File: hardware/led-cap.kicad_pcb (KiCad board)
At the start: 2 copper layers, 76.2 x 50.8 mm, 10 parts, among them IC1 ATTINY20-X, K1 CONN_3, P1 CONN_2, P2 CONN_6, Q1 IRLML2402PbF, U1 MMA7660

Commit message: Cleanup and PCB Layout
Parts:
- C1, C2: footprint SMD_Packages:SM0805 -> SM0805
- IC1: footprint SMD_Packages:TSSOP16 -> TSSOP16
- K1: footprint Connect:SIL-3 -> SIL-3
- P1: footprint Connect:SIL-2 -> SIL-2
- P2: footprint Connect:SIL-6 -> SIL-6
- Q1: footprint SMD_Packages:SOT23 -> SOT23
- R1, R2: footprint SMD_Packages:SM0603 -> SM0603
- U1: footprint tom:DFN-10 -> DFN10
- moved R2 98.3 mm to (61.0, 71.1)
- moved P2 90.3 mm to (55.2, 78.7), turned to 90 degrees
- moved U1 88.1 mm to (66.8, 69.5), turned to 180 degrees
- moved P1 86.8 mm to (75.7, 63.4)
- moved C2 85.4 mm to (75.7, 69.5)
- moved C1 84.6 mm to (75.7, 67.2)
- moved IC1 80.2 mm to (66.8, 77.0)
- moved R1 80.0 mm to (61.0, 73.9)
- moved Q1 76.2 mm to (77.0, 74.9), turned to 270 degrees
- moved K1 67.2 mm to (82.4, 71.1), turned to 270 degrees
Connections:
- IC1 pad 2: Net-(IC1-Pad2) -> (no net)
- IC1 pad 7: Net-(IC1-Pad7) -> (no net)
- IC1 pad 8: Net-(IC1-Pad8) -> (no net)
- U1 pad 1: Net-(U1-Pad1) -> (no net)
- U1 pad 10: Net-(U1-Pad10) -> (no net)
- U1 pad 2: Net-(U1-Pad2) -> (no net)
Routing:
- net VCC: track 0.00 -> 83.4 mm, vias 0 -> 2
- net N-000011: track 0.00 -> 27.0 mm
- net N-000007: track 0.00 -> 20.4 mm
- net N-000010: track 0.00 -> 16.9 mm
- net N-000002: track 0.00 -> 15.8 mm
- net N-000014: track 0.00 -> 15.3 mm
- net N-000006: track 0.00 -> 13.9 mm
- net GND: track 0.00 -> 13.7 mm, vias 0 -> 3
- net N-000001: track 0.00 -> 13.3 mm, vias 0 -> 2
- net N-000009: track 0.00 -> 11.1 mm
- net N-000004: track 0.00 -> 6.72 mm
- net N-000003: track 0.00 -> 4.69 mm
- added copper zone on B.Cu, net GND
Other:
- outline, holes or cut-outs redrawn
- net class Default: trace_width 0.254 -> 0.2032
- rule pad_to_mask_clearance: 0 -> 0.254
- rule trace_min: 0.254 -> 0.2032

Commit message: Preliminary layout
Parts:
- removed P2: CONN_6, SIL-6
- added K2: CONN_3, prgm:bcProgramHeader, F.Cu at (186.9, 71.8)
- added K3: CONN_3, prgm:bcProgramHeader_bottom, F.Cu at (186.9, 71.8)
- C1, C2: footprint SM0805 -> Capacitors_SMD:C_0805_HandSoldering
- IC1: footprint TSSOP16 -> tssop-14:TSSOP14
- K1: footprint SIL-3 -> Connect:GS3; moved to B.Cu
- P1: footprint SIL-2 -> mods.pretty:AA_Box
- Q1: footprint SOT23 -> SMD_Packages:SOT-323
- R1, R2: footprint SM0603 -> Resistors_SMD:R_0603_HandSoldering
- U1: footprint DFN10 -> dfn-10.pretty:DFN-10
- moved IC1 112.4 mm to (179.1, 82.3), turned to 90 degrees
- moved R1 111.3 mm to (172.2, 78.3), turned to 270 degrees
- moved R2 109.9 mm to (170.2, 83.7), turned to 90 degrees
- moved K1 109.4 mm to (191.6, 77.5), turned to 0 degrees
- moved U1 103.1 mm to (169.3, 80.4), turned to 0 degrees
- moved Q1 99.3 mm to (176.3, 76.8)
- moved C2 95.6 mm to (171.2, 73.7)
- moved C1 95.6 mm to (171.2, 71.1)
- moved P1 44.7 mm to (118.1, 77.5)
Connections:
- net N-000001 renamed /Accel_INT
- net N-000002 renamed /LED_DATA
- net N-000003 renamed /LED_GND
- net N-000004 renamed /LED_CTRL
- net N-000009 renamed /SDA
- net N-000010 renamed /SCL
- IC1 pad 2: (no net) -> Net-(IC1-Pad2)
- IC1 pad 3: N-000006 -> /MOSI
- IC1 pad 4: N-000007 -> /RST
- IC1 pad 5: N-000014 -> /MISO
- IC1 pad 6: N-000011 -> /SCLK
- IC1 pad 7: (no net) -> Net-(IC1-Pad7)
- IC1 pad 8: (no net) -> Net-(IC1-Pad8)
- U1 pad 1: (no net) -> Net-(U1-Pad1)
- U1 pad 10: (no net) -> Net-(U1-Pad10)
- U1 pad 2: (no net) -> Net-(U1-Pad2)
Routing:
- net VCC: track 83.4 -> 117.5 mm, vias 2 -> 3
- net N-000011: track 27.0 -> 0.00 mm
- net /MOSI: track 0.00 -> 20.7 mm, vias 0 -> 1
- net N-000007: track 20.4 -> 0.00 mm
- net /MISO: track 0.00 -> 20.1 mm, vias 0 -> 2
- net /RST: track 0.00 -> 19.5 mm, vias 0 -> 1
- net /LED_GND: track 4.69 -> 20.4 mm, vias 0 -> 1
- net N-000014: track 15.3 -> 0.00 mm
- net N-000006: track 13.9 -> 0.00 mm
- net /SCLK: track 0.00 -> 12.7 mm
- net /SCL: track 16.9 -> 8.76 mm
- net /Accel_INT: track 13.3 -> 9.01 mm
- net /LED_DATA: track 15.8 -> 18.5 mm, vias 0 -> 1
- net /SDA: track 11.1 -> 10.4 mm, vias 0 -> 2
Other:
- board size 76.2 x 50.8 mm -> 76.2 x 17.8 mm
- net class Default: clearance 0.254 -> 0.1524; trace_width 0.2032 -> 0.254
- rule pad_to_mask_clearance: 0.254 -> 0
- rule trace_clearance: 0.254 -> 0.1524
- rule trace_min: 0.2032 -> 0.254

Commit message: Just a bit of cleanup
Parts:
- K1: footprint Connect:GS3 -> mods.pretty:GS3
- moved K2 4.70 mm to (182.2, 71.8)
- moved K3 4.70 mm to (182.2, 71.8)
- moved K1 1.14 mm to (190.5, 77.5)
- moved Q1 0.57 mm to (176.0, 77.3)
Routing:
- net VCC: track 117.5 -> 125.8 mm, vias 3 -> 2
- net GND: track 14.2 -> 19.8 mm
- net /RST: track 19.5 -> 14.0 mm
- net /MOSI: track 20.7 -> 16.7 mm
- net /LED_DATA: track 18.5 -> 20.9 mm, vias 1 -> 3
- net /LED_GND: track 20.4 -> 18.7 mm, vias 1 -> 3
- net /LED_CTRL: track 6.49 -> 4.95 mm
- net /MISO: track 20.1 -> 18.9 mm

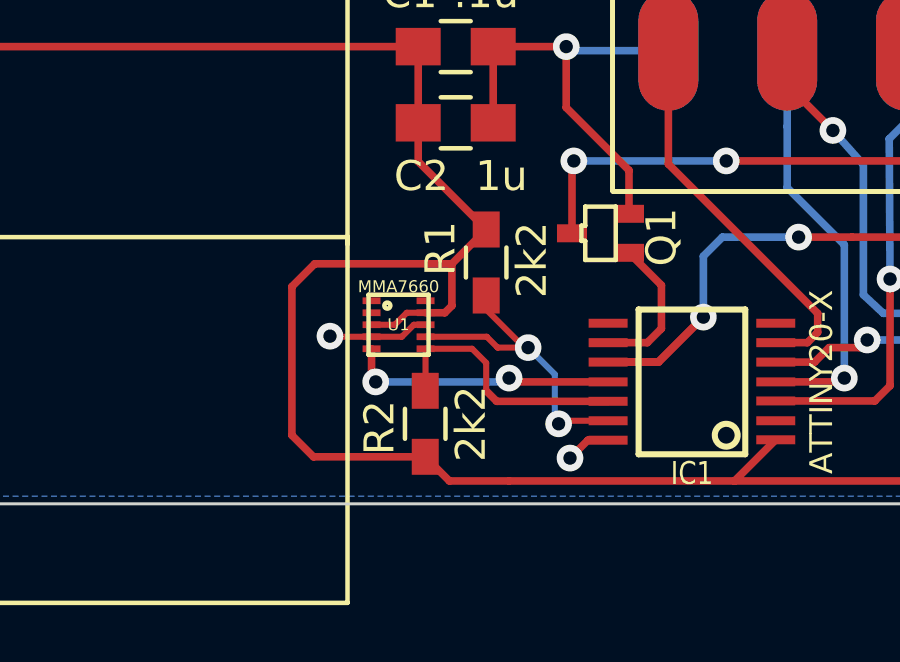
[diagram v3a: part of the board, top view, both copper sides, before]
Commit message: Using will's part of the accel
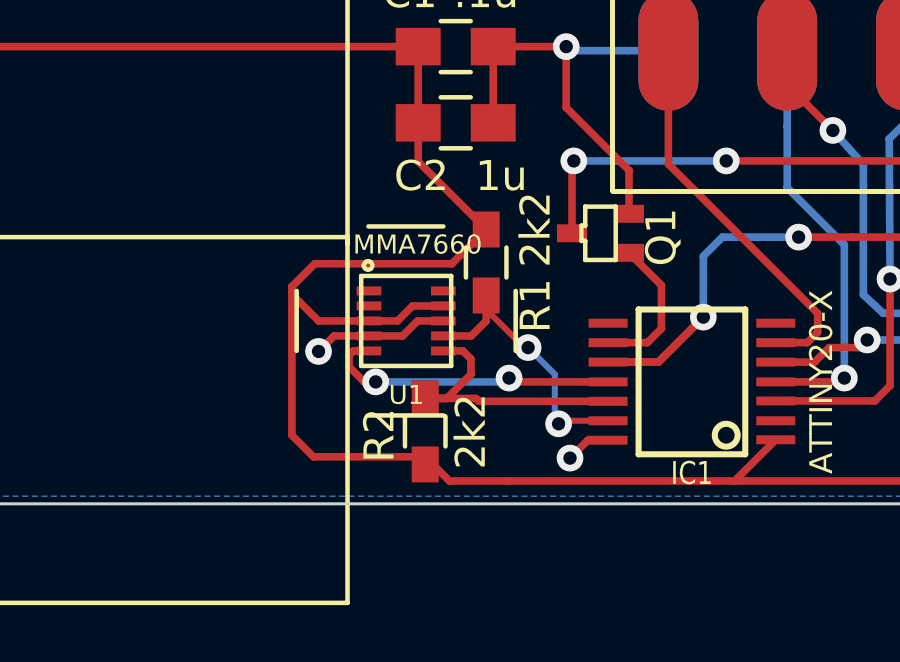
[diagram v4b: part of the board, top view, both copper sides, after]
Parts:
- U1: footprint dfn-10.pretty:DFN-10 -> dfn-10:MMA7660FC
- moved U1 0.28 mm to (169.5, 80.3), turned to 270 degrees
- moved R2 0.25 mm to (170.2, 83.9)
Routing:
- net VCC: track 125.8 -> 127.4 mm
- net /Accel_INT: track 9.01 -> 10.3 mm
- net GND: track 19.8 -> 21.0 mm
- net /SDA: track 10.4 -> 9.40 mm
- net /SCL: track 8.76 -> 9.55 mm

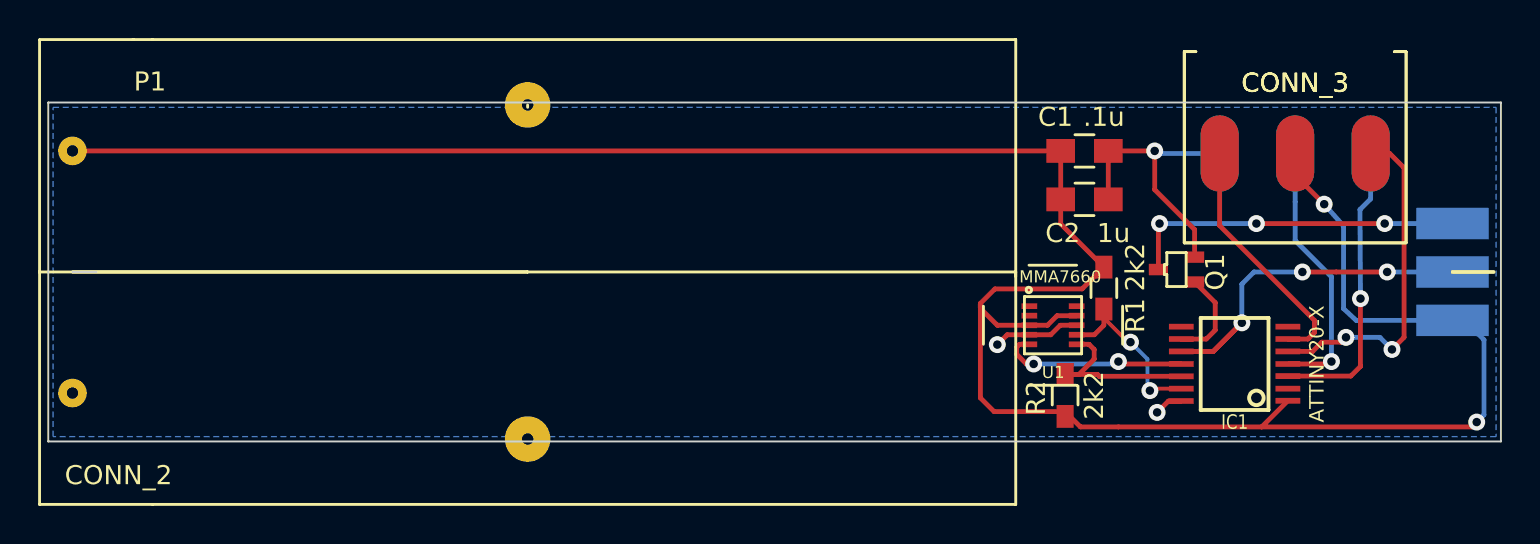
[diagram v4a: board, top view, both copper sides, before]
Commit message: Updating based on Sheaff & Segee recommendations
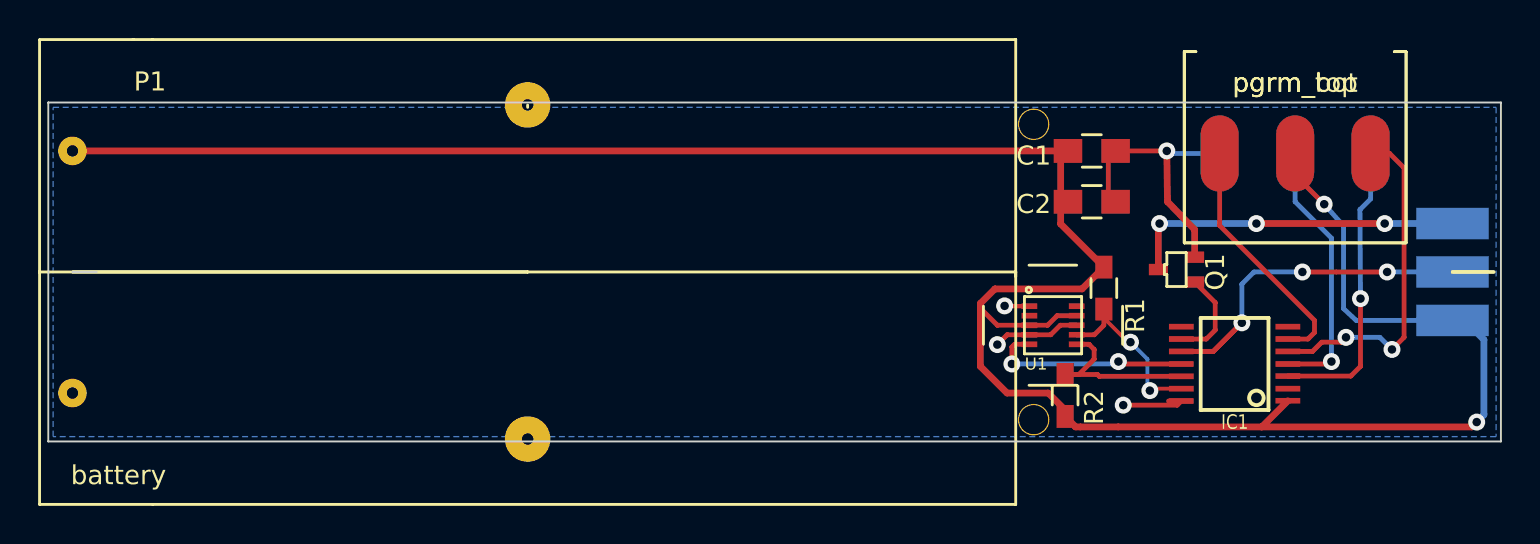
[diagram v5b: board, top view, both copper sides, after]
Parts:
- added 1pin: VAL**, mods.pretty:1pin, F.Cu at (168.5, 69.7)
- added 1pin: VAL**, mods.pretty:1pin, F.Cu at (168.5, 85.2)
- K2: value CONN_3 -> pgrm_top
- K3: value CONN_3 -> pgrm_bot
- P1: value CONN_2 -> battery
- moved C2 0.40 mm to (171.6, 73.8)
- moved C1 0.38 mm to (171.6, 71.1)
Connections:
- U1 pad 1: Net-(U1-Pad1) -> GND
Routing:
- net GND: track 21.0 -> 24.4 mm, vias 3 -> 4
- net /Accel_INT: track 10.3 -> 11.1 mm
- net VCC: track 127.4 -> 126.6 mm
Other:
- rule trace_min: 0.254 -> 0.1524
- board text added: "UMAINE ECE 498 Spring 2015 Butler Fund"

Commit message: Moving parts away from accelerometer
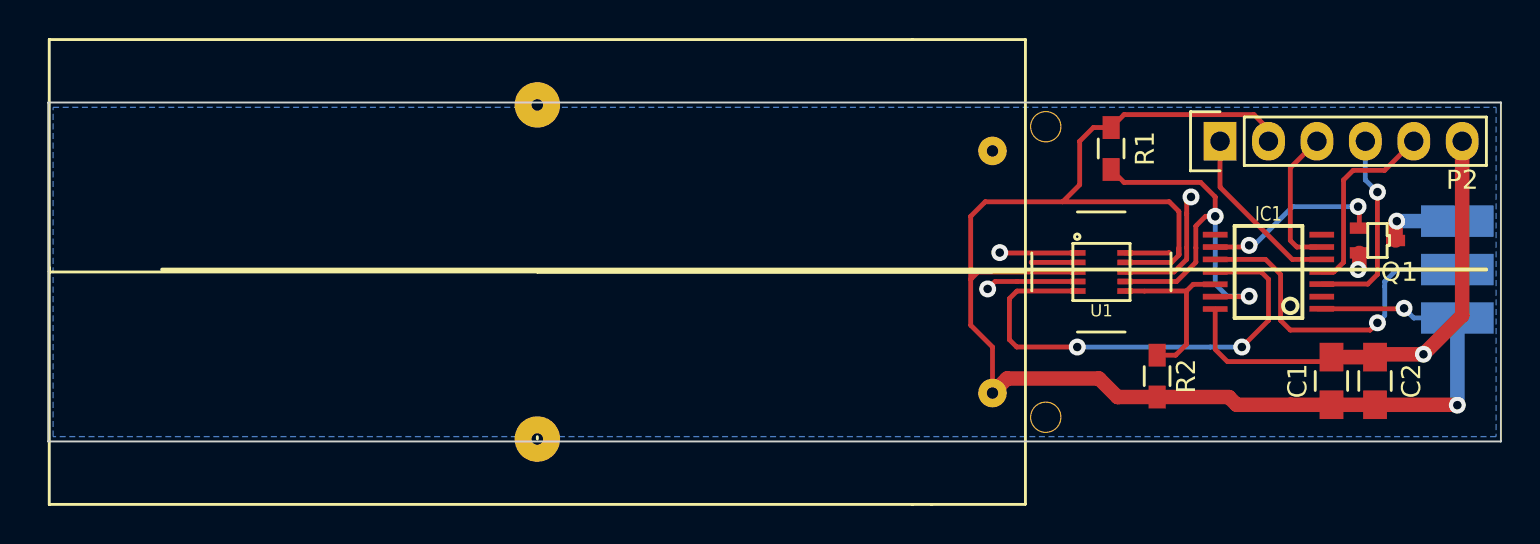
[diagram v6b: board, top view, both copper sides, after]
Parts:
- removed K2: pgrm_top, prgm:bcProgramHeader
- removed K3: pgrm_bot, prgm:bcProgramHeader_bottom
- added P2: pgrm, Pin_Headers:Pin_Header_Straight_1x06, F.Cu at (178.3, 70.6)
- moved P1 48.3 mm to (166.4, 77.5), turned to 180 degrees
- moved C2 17.6 mm to (186.4, 83.2), turned to 90 degrees
- moved C1 17.4 mm to (184.2, 83.2), turned to 90 degrees
- moved Q1 10.7 mm to (186.6, 75.8), turned to 90 degrees
- moved R1 7.33 mm to (172.6, 71.0)
- moved IC1 5.14 mm to (180.8, 77.5)
- moved R2 4.93 mm to (175.0, 82.9)
- moved U1 3.78 mm to (172.1, 77.5)
- moved 1pin 0.65 mm to (169.2, 69.8)
- moved 1pin 0.65 mm to (169.2, 85.1)
- moved K1 0.28 mm to (190.8, 77.3)
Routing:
- net VCC: track 126.6 -> 85.1 mm
- net GND: track 24.4 -> 42.3 mm, vias 4 -> 5
- net /LED_GND: track 18.7 -> 4.22 mm, vias 3 -> 1
- net /Accel_INT: track 11.1 -> 25.3 mm
- net /SDA: track 9.40 -> 21.7 mm
- net /MISO: track 18.9 -> 9.31 mm, vias 2 -> 0
- net /MOSI: track 16.7 -> 10.4 mm
- net /SCLK: track 13.0 -> 7.32 mm
- net /LED_CTRL: track 4.95 -> 9.65 mm, vias 0 -> 2
- net /RST: track 14.0 -> 10.2 mm, vias 1 -> 0
- net Net-(U1-Pad2): track 0.00 -> 2.45 mm
- net Net-(U1-Pad10): track 0.00 -> 2.32 mm
- net /LED_DATA: track 20.9 -> 20.5 mm, vias 3 -> 1
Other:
- outline, holes or cut-outs redrawn
